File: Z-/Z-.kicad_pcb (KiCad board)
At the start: 4 copper layers, 98 x 98 mm, 154 parts, among them J1 200528-0100, J2 U.FL, J3 U.FL, J5 Conn_01x02, K1 IM11DGR, Q1 NX3008NBKS, Q10 MBT2222ADW1T1, Q11 NX3008NBKS, Q12 MBT2222ADW1T1, Q13 NX3008NBKS, Q14 MBT2222ADW1T1, Q15 IRFTS9342PBF, Q16 NX3008NBKS, Q17 IRFTS9342PBF, Q18 MBT2222ADW1T1, Q19 IRFTS9342PBF, Q2 MBT2222ADW1T1, Q20 IRLML2803, Q21 SiRA99DP, Q3 NX3008NBKS, Q4 MBT2222ADW1T1, Q5 NX3008NBKS, Q6 MBT2222ADW1T1, Q7 NX3008NBKS, Q8 MBT2222ADW1T1, Q9 NX3008NBKS, U1 OPT4003DNPRQ1, U2 PCA9633DP2, U3 ADM1176-1ARMZ-R7, U4 DRV8235RTER

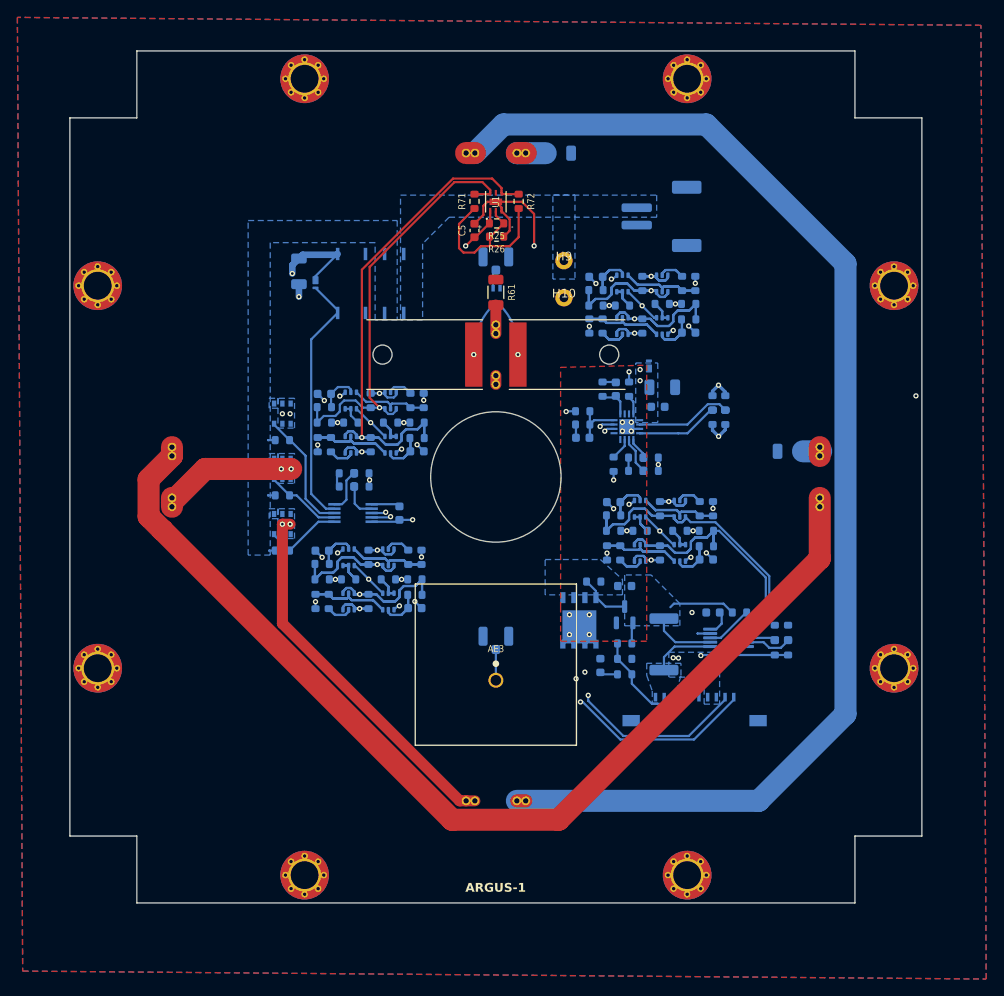
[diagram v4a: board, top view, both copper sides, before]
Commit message: Updated schematics/layout with mainboard compatability
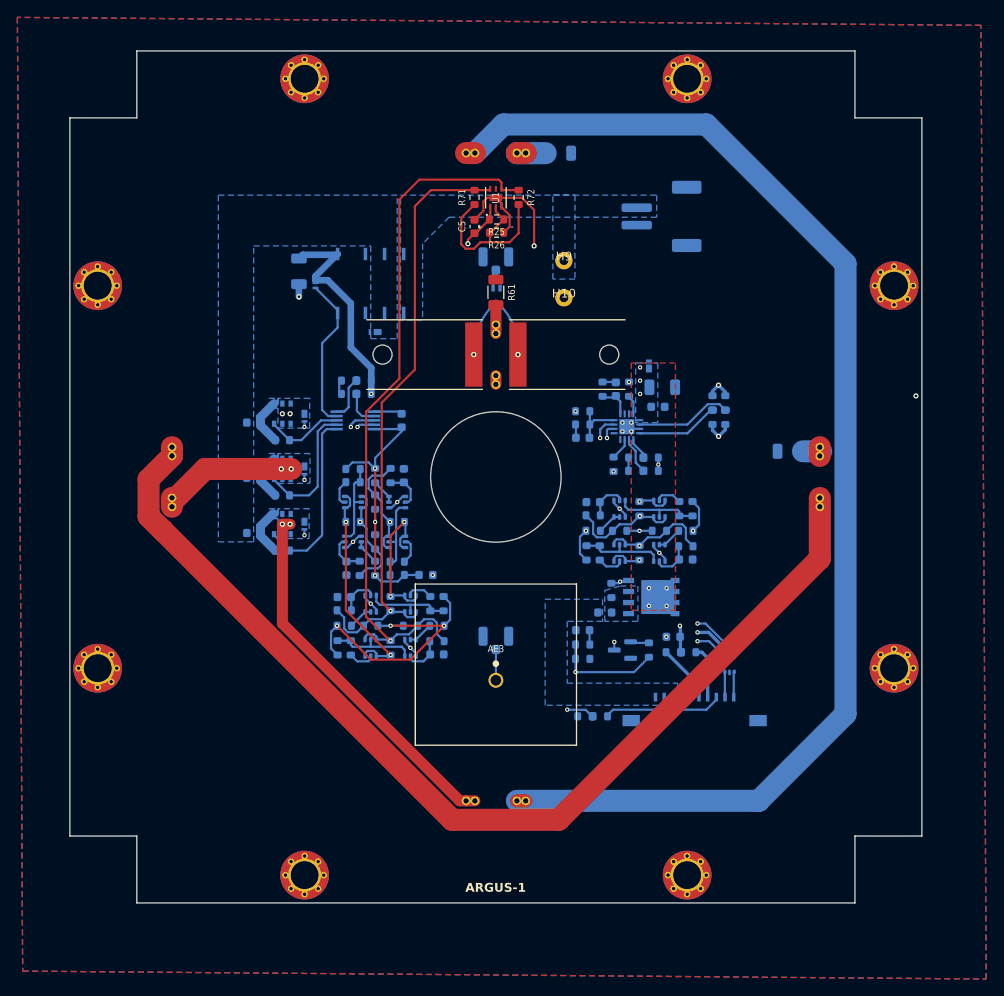
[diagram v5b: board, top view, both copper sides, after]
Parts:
- removed C12, C14, C15: 10nF, Capacitor_SMD:C_0603_1608Metric
- removed Q13, Q16: NX3008NBKS, Package_TO_SOT_SMD:SOT-363_SC-70-6
- removed Q14, Q18: MBT2222ADW1T1, Package_TO_SOT_SMD:SOT-363_SC-70-6
- removed R68, R76, R84: 680R, Resistor_SMD:R_0603_1608Metric
- removed R69, R77, R85: 100K, Resistor_SMD:R_0603_1608Metric
- removed R70, R78, R86: DNI (0R), Resistor_SMD:R_0603_1608Metric
- removed R73, R74, R79, R82, R87, R88: 10K, Resistor_SMD:R_0603_1608Metric
- removed R75, R83, R89: 200K, Resistor_SMD:R_0603_1608Metric
- removed U3: ADM1176-1ARMZ-R7, Package_SO:MSOP-10_3x3mm_P0.5mm
- added D4: 10V, Diode_SMD:Nexperia_DSN1608-2_1.6x0.8mm, B.Cu at (130.3, 94.7)
- added D5: 10V, Diode_SMD:Nexperia_DSN1608-2_1.6x0.8mm, B.Cu at (130.3, 101.1)
- added D6: 10V, Diode_SMD:Nexperia_DSN1608-2_1.6x0.8mm, B.Cu at (130.3, 88.7)
- added D7: 10V, Diode_SMD:Nexperia_DSN1608-2_1.6x0.8mm, B.Cu at (138.4, 79.0)
- added F2: 500mA, Fuse:Fuse_0603_1608Metric, B.Cu at (144.3, 106.9)
- added F3: 500mA, Fuse:Fuse_0603_1608Metric, B.Cu at (172.7, 114.0)
- added F4: 500mA, Fuse:Fuse_0603_1608Metric, B.Cu at (124.5, 89.4)
- added F5: 500mA, Fuse:Fuse_0603_1608Metric, B.Cu at (124.5, 102.1)
- added F6: 500mA, Fuse:Fuse_0603_1608Metric, B.Cu at (124.5, 95.8)
- added R47: 0R, Resistor_SMD:R_0603_1608Metric, B.Cu at (164.3, 123.2)
- added R48: 0R, Resistor_SMD:R_0603_1608Metric, B.Cu at (162.6, 123.2)
- added R80: 0R, Resistor_SMD:R_0603_1608Metric, B.Cu at (172.7, 115.8)
- added R81: 0R, Resistor_SMD:R_0603_1608Metric, B.Cu at (174.5, 115.8)
- added U5: USBLC6-2P6, Package_TO_SOT_SMD:SOT-666, B.Cu at (179.2, 117.2)
- C6: value 3.3nF -> 10nF
- R10, R62: value 0R -> 200K
- R14, R30, R40, R54: value 10K -> 680R
- R17, R31, R42: value 10K -> 100K
- R18, R32, R45: value 200K -> DNI (0R)
- R2: value ?R -> 100K; footprint Resistor_SMD:R_2512_6332Metric -> Resistor_SMD:R_0603_1608Metric
- R27, R33, R46: value 680R -> 10K
- R28, R34, R50: value 100K -> 10K
- R29, R38, R52: value DNI (0R) -> 200K
- R3: value 100K -> DNI (0R)
- R4: value 1K -> 10K
- R5: value DNI (0R) -> 10K
- R56: value 0R -> 100K
- R57: value 10K -> DNI (0R)
- R58: value 200K -> 10K
- R59: value 0R -> 10K
- moved R10 49.7 mm to (134.9, 111.0), turned to 0 degrees
- moved R42 42.2 mm to (174.2, 101.9)
- moved R2 36.8 mm to (134.9, 112.8), turned to 0 degrees
- moved R45 36.5 mm to (168.8, 104.4), turned to -90 degrees
- moved R4 34.1 mm to (146.3, 110.2), turned to -90 degrees
- moved C2 32.7 mm to (145.5, 116.1), turned to 0 degrees
- moved R22 30.1 mm to (134.1, 115.3), turned to 90 degrees
- moved R24 29.9 mm to (145.5, 114.6), turned to 180 degrees
- moved Q3 29.3 mm to (142.5, 115.3), turned to -90 degrees
- moved R19 29.3 mm to (135.6, 115.3), turned to 90 degrees
- moved Q4 28.5 mm to (137.9, 115.3), turned to 90 degrees
- moved R21 28.5 mm to (140.2, 115.3), turned to -90 degrees
- moved R46 26.2 mm to (162.7, 104.4)
- moved R62 26.2 mm to (163.5, 100.1), turned to 0 degrees
- moved Q10 26.1 mm to (166.6, 104.4)
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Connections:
- C11 pad 1: Net-(Q9B-G1) -> Net-(Q11B-G1)
- C13 pad 1: 3.3V -> BW_3V3
- C16 pad 1: 3.3V -> PERI_3V3
- C5 pad 1: 3.3V -> LS_3V3
- C6 pad 1: GND -> Net-(Q9B-G1)
- C6 pad 2: Net-(U3-TIMER) -> GND
- D1 pad 1: 3.3V -> PERI_3V3
- F1 pad 2: VDRIVE -> VBATT_SENSE
- J1 pad 1: SCL -> Net-(J1-Pin_1)
- J1 pad 2: SDA -> Net-(J1-Pin_2)
- J1 pad 3: 3.3V -> /COIL_DRIVER_EN_OR_MAIN_3V3
- J1 pad 4: 3.3V -> MAIN_3V3
- J1 pad 5: GND -> /PERI_3V3_OR_GND
- J1 pad 7: COIL_DRIVER_EN -> GND
- K1 pad 1: 3.3V -> PERI_3V3
- Q15 pad 4: /Burn Wires/VBURN_A_IN -> Net-(Q15-S)
- Q17 pad 4: /Burn Wires/VBURN_A_IN -> Net-(Q17-S)
- Q19 pad 4: /Burn Wires/VBURN_A_IN -> Net-(Q19-S)
- Q2 pad 1: SCL -> SDA
- Q2 pad 3: SCL -> SDA
- Q2 pad 4: SCL_LS -> SDA_LS
- Q2 pad 6: SCL_LS -> SDA_LS
- Q4 pad 1: SDA -> SCL
- Q4 pad 3: SDA -> SCL
- Q4 pad 4: SDA_LS -> SCL_LS
- Q4 pad 6: SDA_LS -> SCL_LS
- R10 pad 1: /I2C Devices/A0_CPWR -> SDA_LS
- R10 pad 2: 3.3V -> Net-(Q1B-G1)
- R11 pad 2: 3.3V -> PERI_3V3
- R13 pad 2: 3.3V -> PERI_3V3
- R14 pad 1: 3.3V -> Net-(Q6A-B1)
- R14 pad 2: Net-(Q1A-D1) -> Net-(Q5A-D1)
- R17 pad 1: 3.3V -> BW_3V3
- R17 pad 2: SCL_LS -> Net-(Q5A-G2)
- R18 pad 1: SCL_LS -> SCL_IO
- R18 pad 2: Net-(Q1B-G1) -> SCL
- R2 pad 1: VDRIVE -> LS_3V3
- R2 pad 2: VBATT_SENSE -> Net-(Q1A-G2)
- R20 pad 1: 3.3V -> LS_3V3
- R21 pad 1: SDA_LS -> SCL_LS
- R21 pad 2: SDA -> SCL
- R22 pad 1: 3.3V -> LS_3V3
- R23 pad 1: 3.3V -> LS_3V3
- R23 pad 2: SDA_LS -> SCL_LS
- R24 pad 1: SDA_LS -> SCL_LS
- R25 pad 2: 3.3V -> LS_3V3
- R27 pad 1: Net-(Q6A-B1) -> BW_3V3
- R28 pad 1: 3.3V -> BW_3V3
- R28 pad 2: Net-(Q5A-G2) -> SCL_IO
- R29 pad 2: SCL -> Net-(Q5B-G1)
- R3 pad 1: 3.3V -> SDA_LS
- R3 pad 2: Net-(Q1A-G2) -> SDA
- R30 pad 1: 3.3V -> Net-(Q8A-B1)
- R30 pad 2: Net-(Q5A-D1) -> Net-(Q7A-D1)
- R31 pad 1: 3.3V -> BW_3V3
- R31 pad 2: SCL_IO -> Net-(Q7A-G2)
- R32 pad 1: SCL_IO -> SDA_IO
- R32 pad 2: Net-(Q5B-G1) -> SDA
- R33 pad 1: Net-(Q8A-B1) -> BW_3V3
- R34 pad 1: 3.3V -> BW_3V3
- R34 pad 2: Net-(Q7A-G2) -> SDA_IO
- R38 pad 2: SDA -> Net-(Q7B-G1)
- R39 pad 2: 3.3V -> MAIN_3V3
- R4 pad 1: VDRIVE -> LS_3V3
- R4 pad 2: Net-(U3-ON) -> Net-(Q1A-D1)
- R40 pad 1: 3.3V -> Net-(Q10A-B1)
- R40 pad 2: Net-(Q7A-D1) -> Net-(Q10B-B2)
- R42 pad 1: 3.3V -> MAIN_3V3
- R42 pad 2: SDA_IO -> Net-(Q9A-G2)
- R43 pad 2: /Burn Wires/VBURN_A_IN -> Net-(Q15-S)
- R45 pad 1: SDA_IO -> SCL_M
- R45 pad 2: Net-(Q7B-G1) -> SCL
- R46 pad 1: Net-(Q10A-B1) -> MAIN_3V3
- R49 pad 2: 3.3V -> MAIN_3V3
- R5 pad 1: SCL_LS -> LS_3V3
- R5 pad 2: SCL -> SDA_LS
- R50 pad 1: 3.3V -> MAIN_3V3
- R50 pad 2: Net-(Q9A-G2) -> SCL_M
- R52 pad 2: SCL -> Net-(Q9B-G1)
- R53 pad 2: /Burn Wires/VBURN_A_IN -> Net-(Q17-S)
- R54 pad 1: 3.3V -> Net-(Q12A-B1)
- R54 pad 2: Net-(Q10B-B2) -> Net-(Q11A-D1)
- R56 pad 1: GND -> MAIN_3V3
- R56 pad 2: /I2C Devices/A0_CPWR -> Net-(Q11A-G2)
- R57 pad 1: 3.3V -> SDA_M
- R57 pad 2: SCL_M -> SDA
- R58 pad 1: SCL_M -> MAIN_3V3
- R58 pad 2: Net-(Q9B-G1) -> Net-(Q11A-D1)
- R59 pad 1: /I2C Devices/A1_CPWR -> MAIN_3V3
- R59 pad 2: 3.3V -> SDA_M
- R60 pad 2: /Burn Wires/VBURN_A_IN -> Net-(Q19-S)
- R62 pad 1: GND -> SDA_M
- R62 pad 2: /I2C Devices/A1_CPWR -> Net-(Q11B-G1)
- R63 pad 1: 3.3V -> MAIN_3V3
- R64 pad 1: 3.3V -> MAIN_3V3
- R67 pad 2: 3.3V -> PERI_3V3
- U1 pad 1: 3.3V -> LS_3V3
- U2 pad 10: 3.3V -> BW_3V3
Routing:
- net LS_3V3: track 0.00 -> 121.3 mm, vias 0 -> 5
- net PERI_3V3: track 0.00 -> 101.3 mm, vias 0 -> 4
- net MAIN_3V3: track 0.00 -> 79.0 mm, vias 0 -> 7
- net SDA: track 161.1 -> 88.4 mm, vias 5 -> 4
- net SCL: track 154.7 -> 83.3 mm, vias 5 -> 4
- net 3.3V: track 64.6 -> 0.00 mm, vias 27 -> 0
- net SDA_CPWR: track 47.6 -> 0.00 mm
- net SCL_CPWR: track 42.6 -> 0.00 mm
- net BW_3V3: track 0.00 -> 34.1 mm, vias 0 -> 3
- net SDA_M: track 46.6 -> 25.2 mm
- net SDA_LS: track 50.7 -> 70.9 mm
- net Net-(Q16A-D1): track 18.1 -> 0.00 mm
- net Net-(Q13A-D1): track 18.1 -> 0.00 mm
- net GND: track 65.1 -> 47.3 mm, vias 29 -> 15
- net VDRIVE: track 15.0 -> 0.00 mm
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- added copper zone on In1.Cu, net GND
- removed copper zone on B.Cu, net 3.3V
- removed copper zone on In1.Cu, net 3.3V
- removed copper zone on B.Cu, net VDRIVE

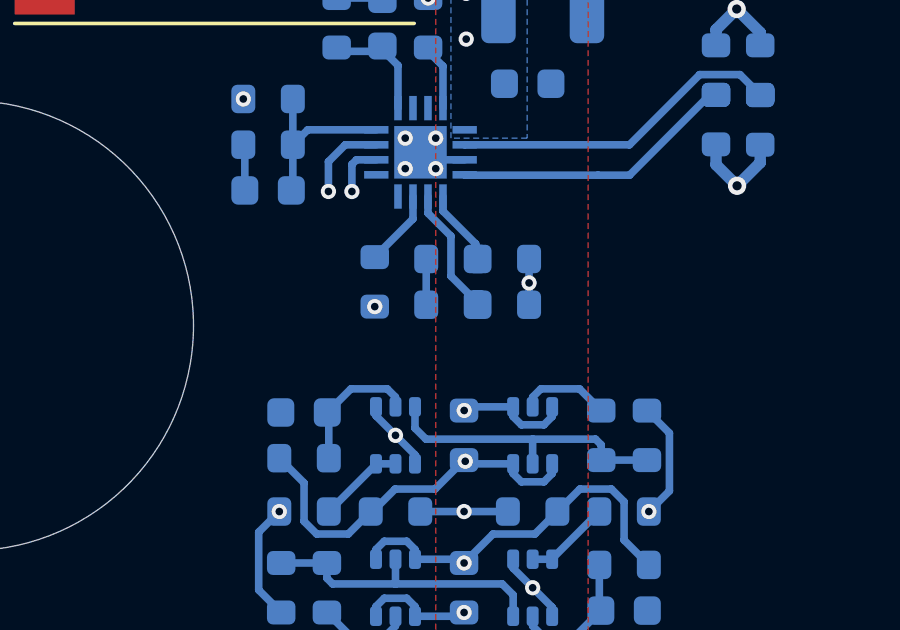
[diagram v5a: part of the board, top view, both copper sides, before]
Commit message: Moved coil driver fully onto main 3v3
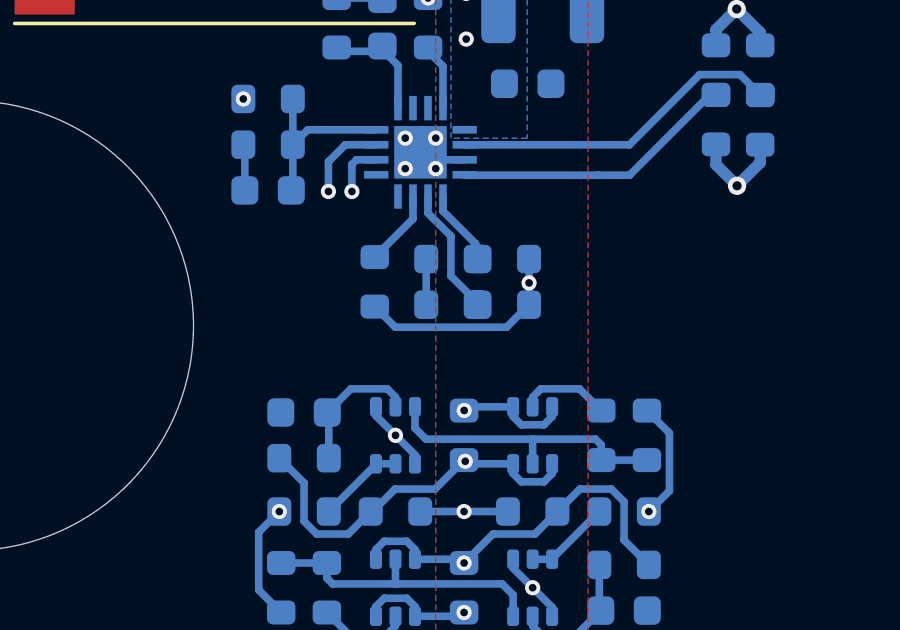
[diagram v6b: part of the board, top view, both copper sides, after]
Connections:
- R67 pad 2: PERI_3V3 -> MAIN_3V3
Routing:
- net PERI_3V3: track 101.3 -> 84.5 mm, vias 4 -> 3
- net MAIN_3V3: track 79.0 -> 84.7 mm

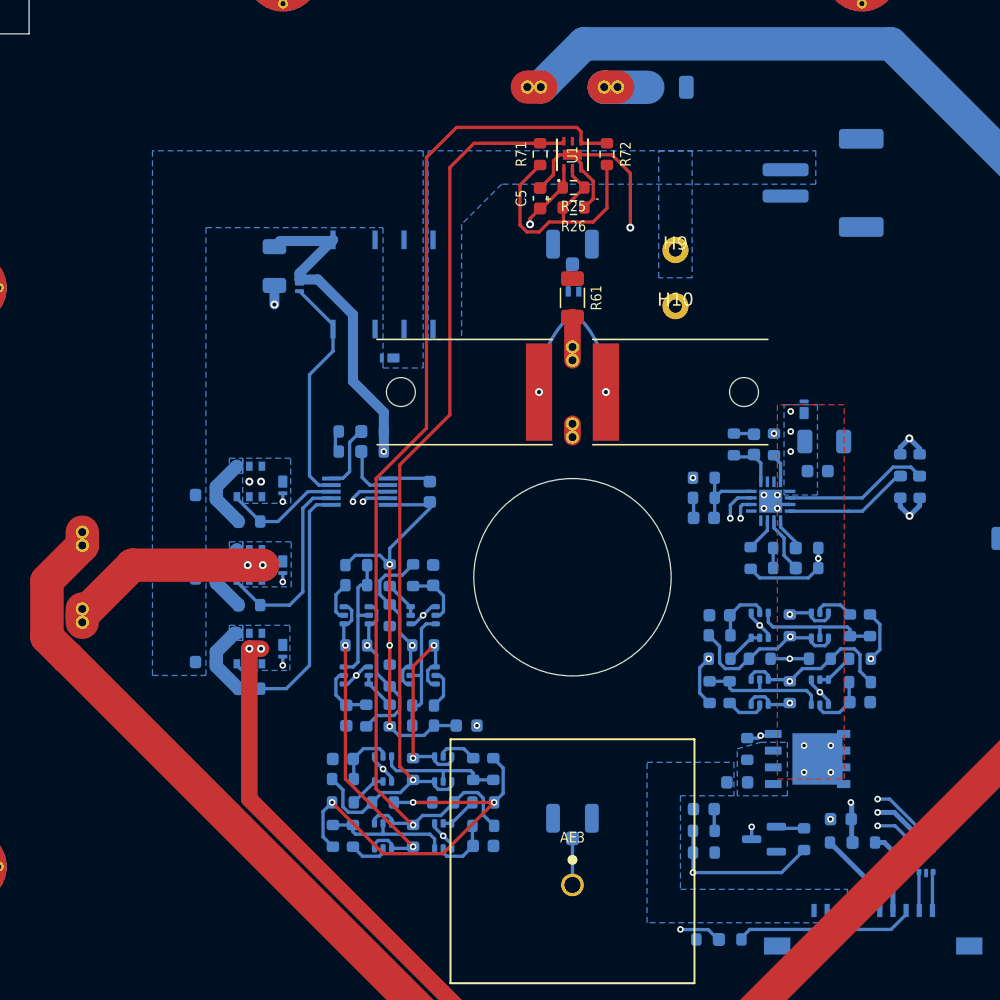
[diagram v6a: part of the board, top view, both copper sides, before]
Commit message: Added via stitching
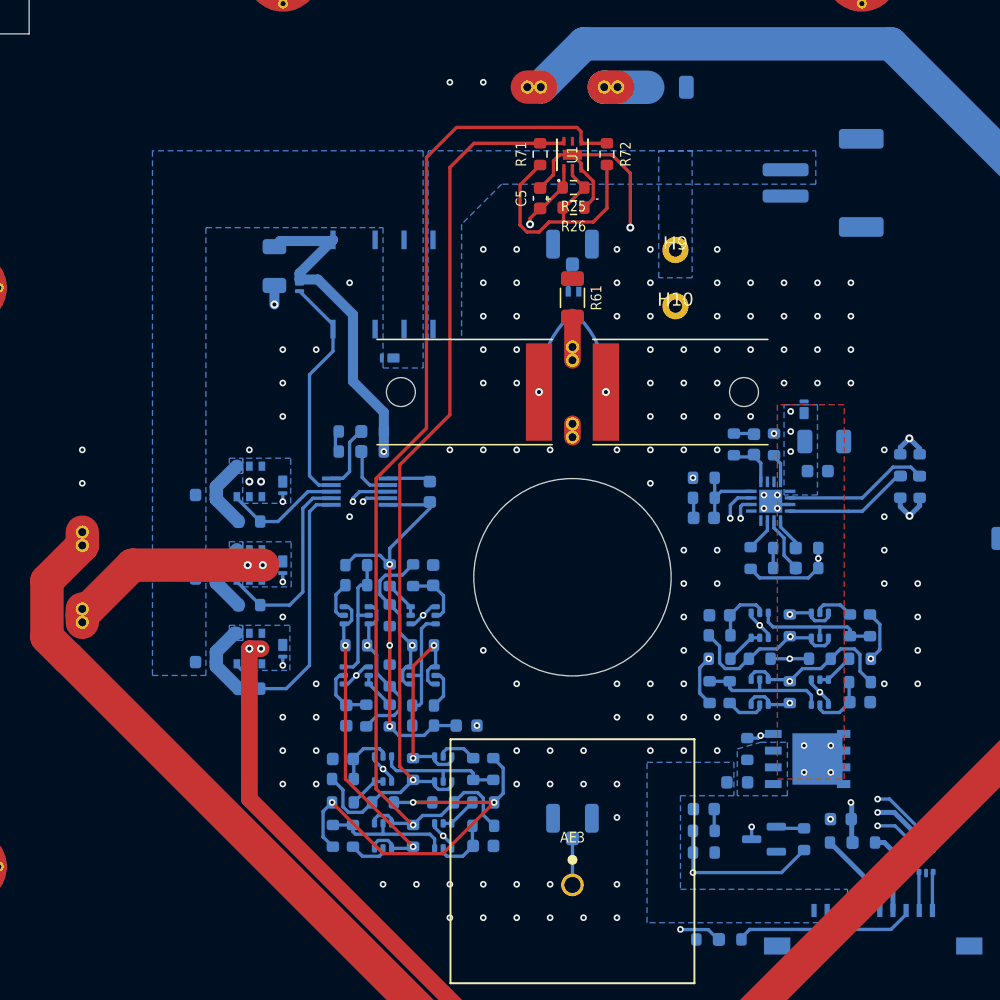
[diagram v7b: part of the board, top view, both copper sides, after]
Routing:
- net GND: vias 15 -> 135
